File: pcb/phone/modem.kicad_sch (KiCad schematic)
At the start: 5 parts, among them U2 PCIE-52P40H_C444926, U8 TXB0108PWR

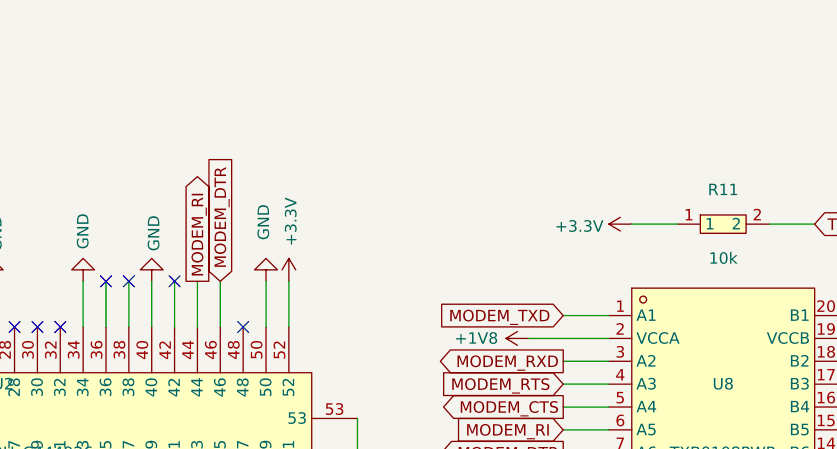
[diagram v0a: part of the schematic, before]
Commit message: Add deferred components: VBUS divider, MCU_MODEM_PWR_EN pull-down, SWD header, NET_STATUS LED
MCU sheet:
- R11 (10k): MCU_MODEM_PWR_EN pull-down to GND
- R12 (100k) + R13 (47k): VBUS_SENSE voltage divider from VBUS to GND
- J3 (Conn_01x04): SWD programming header (SWCLK, SWDIO, +3.3V, GND)
- Removed 4 no_connect markers (MCU_MODEM_PWR_EN, VBUS_SENSE, SWCLK, SWDIO)

Modem sheet:
- R12 (1k) + LED1 (LTST-C191TBKT): NET_STATUS indicator LED
- Removed 1 no_connect marker (NET_STATUS)

ERC: 0 errors, 4 warnings (all lib_symbol_mismatch — 3 pre-existing + 1 new for J3)

Generated with [Devin](https://devin.ai)

Co-Authored-By: Devin <158243242+devin-ai-integration[bot]@users.noreply.github.com>
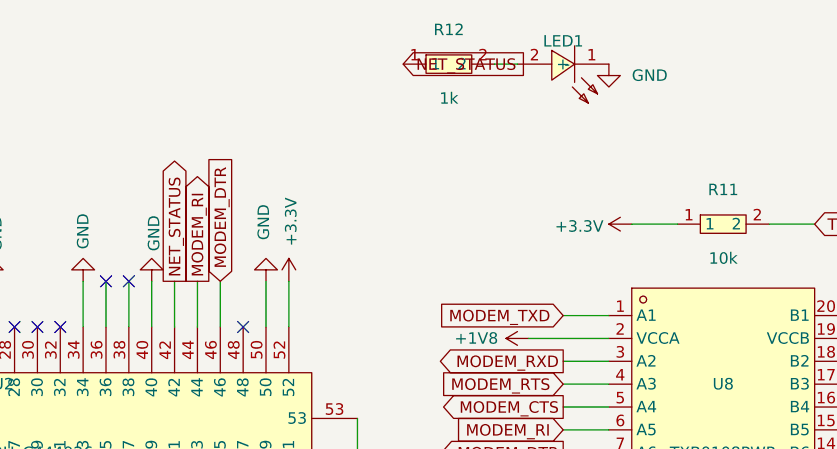
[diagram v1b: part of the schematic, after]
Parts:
- added LED1: LTST-C191TBKT, easyeda2kicad:LED0603-RD, symbol passives:LTST-C191TBKT
- added R12: 1k, symbol passives:RC0603JR-0710KL
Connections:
- net GND: now also LED1.1 (-)
- net NET_STATUS: now reaches U2.42
- net NET_STATUS: now also R12.1
- new net: LED1.2 (+), R12.2
- no-connect marks 17 -> 16

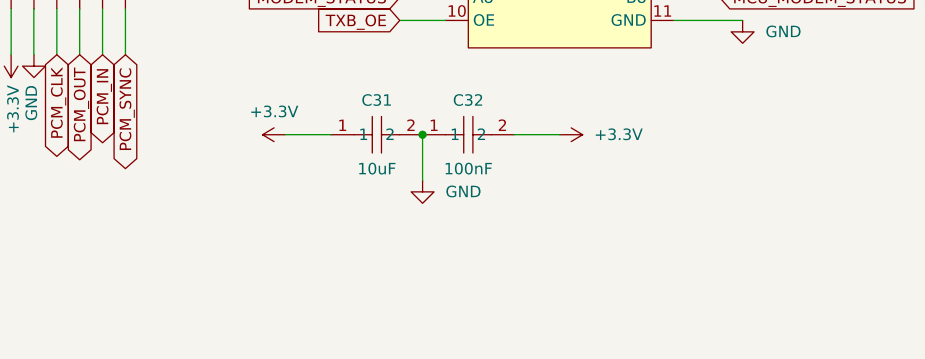
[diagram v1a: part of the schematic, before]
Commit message: Add power slide switch, modem bulk caps, reverse load switch decision
- SW1 (ALPS SSSS811101) added to power sheet: controls TPS63021 EN pin
  (ON: +BATT->R1->SW1->EN, OFF: EN->SW1->GND). Allows charging while off.
- C40 (470uF tantalum) + C41/C42 (10uF ceramic) added to modem sheet
  near MPCIe VCC pins for 2A+ LTE burst handling.
- Reversed load switch decision: SIM7600 sleep mode + PWRKEY make it
  redundant. Removed R11 (MCU_MODEM_PWR_EN pull-down), added no_connect
  on PE6.
- Registered temp_switch/temp_470uf/temp_10uf libraries in sym-lib-table
  and fp-lib-table (resolves 3 library-link ERC warnings).
- Final ERC: 0 errors, 6 warnings (all lib_symbol_mismatch, harmless).
- Updated docs: project-log, task-tracker, bom.

Generated with [Devin](https://devin.ai)

Co-Authored-By: Devin <158243242+devin-ai-integration[bot]@users.noreply.github.com>
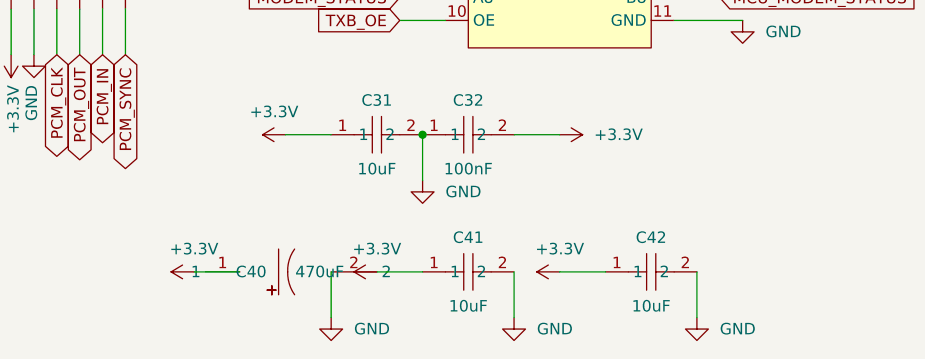
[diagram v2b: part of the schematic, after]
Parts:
- added C40: 470uF, symbol temp_470uf:6TPF470MAH
- added C41, C42: 10uF, symbol passives:GRM21BR61H106KE43L
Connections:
- net +3.3V: now also C40.1, C41.1, C42.1
- net GND: now also C40.2, C41.2, C42.2

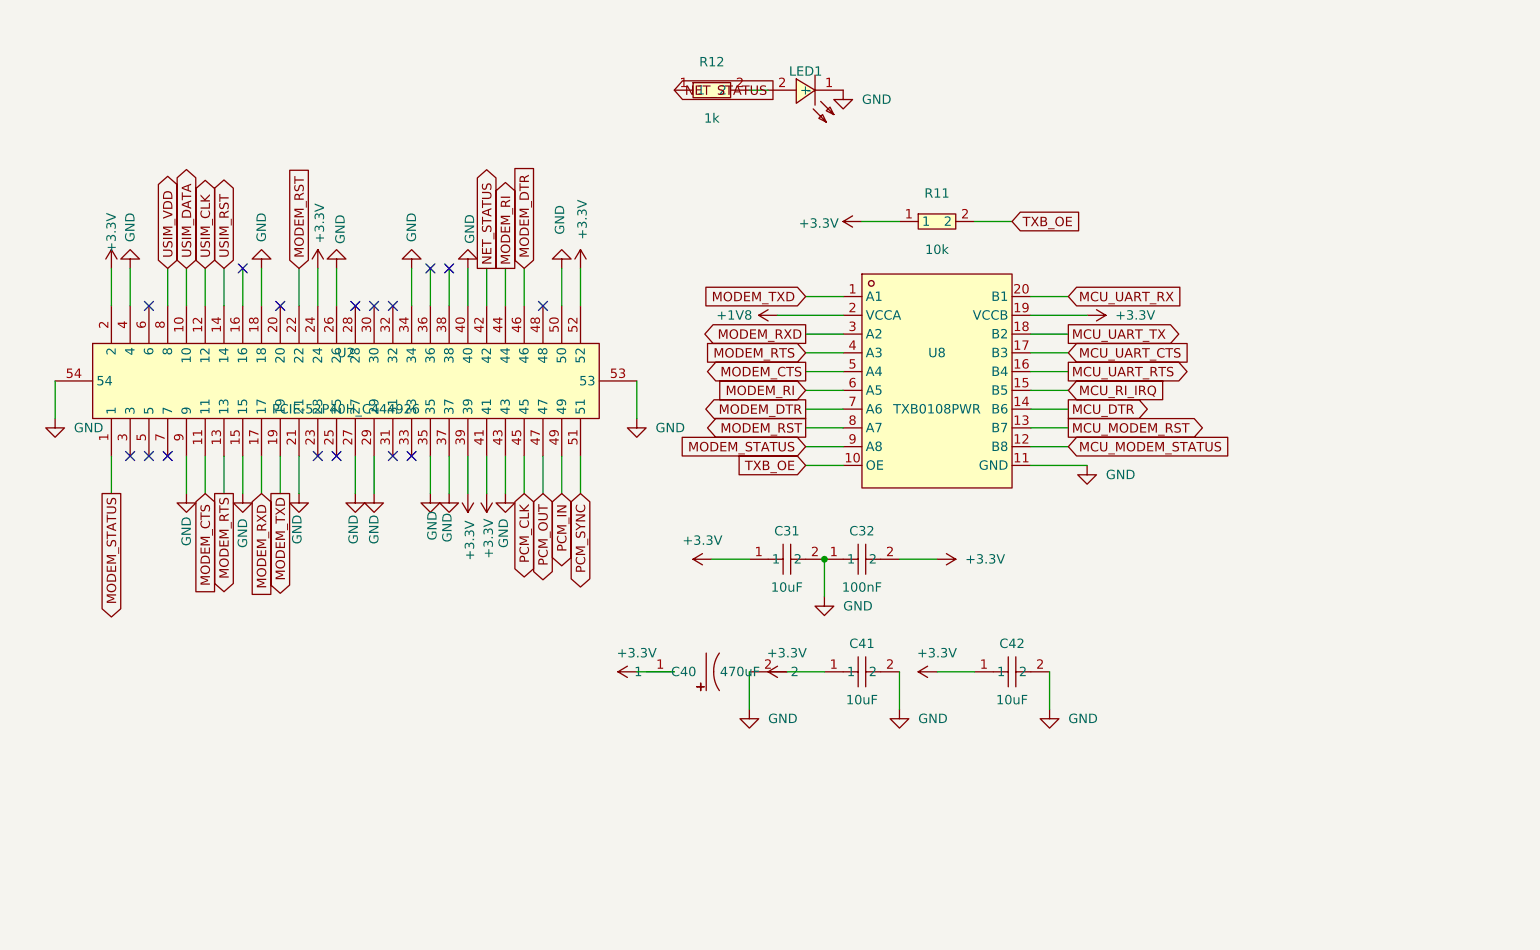
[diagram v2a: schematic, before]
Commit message: Cleanup: remove rejected part symbols, one-off scripts, stale datasheets
- Remove 7 rejected symbols from easyeda2kicad.kicad_sym (PJ-327C-4A,
  PJ-3250-5A, PJ-3240-5A, TYPE-C16PLC-H10.0, PJ-327A5JJ, PJ-327-P5,
  TYPEC-306DDW-ARP16) — replaced by Tensility 54-00298 and GCT USB4085-GF-A
- Delete 10 one-off inspection scripts (check_*.py, find_*.py, dump_*.py,
  extract_*.py) — keep only gen_*.py schematic generators
- Delete rejected datasheets (pj3126-5a, pj3240-5a, pj3250-5a, pj3f07-5p,
  N114 superseded display)
- Delete generated BOM/POS CSV files
- Add alps-ssss2.pdf and gct-usb4085.pdf to reference README index
- Include all schematic changes from previous sessions (SD pullups, VBUS
  divider fix, level shifter verification, codec caps, DCVDD fix)

Generated with [Devin](https://devin.ai)

Co-Authored-By: Devin <158243242+devin-ai-integration[bot]@users.noreply.github.com>
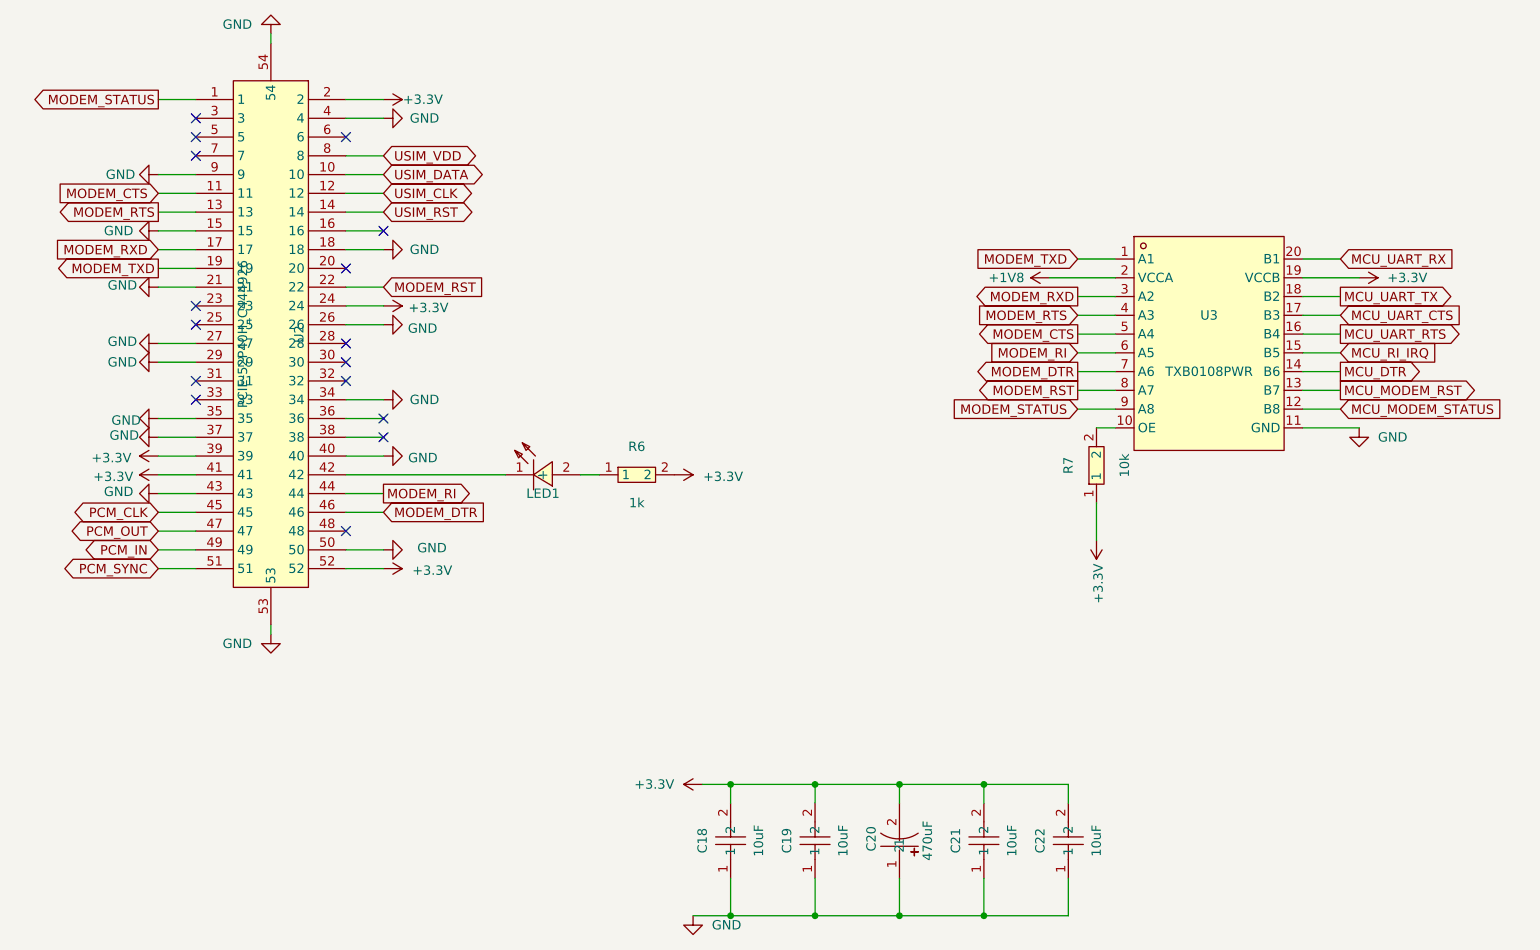
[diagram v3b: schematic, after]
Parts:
- removed C31, C41, C42: 10uF, symbol passives:GRM21BR61H106KE43L
- removed C32: 100nF, symbol passives:CC0603KRX7R9BB104
- removed C40: 470uF, symbol temp_470uf:6TPF470MAH
- added C18, C19, C21, C22: 10uF, symbol passives:GRM21BR61H106KE43L
- added C20: 470uF, symbol temp_470uf:6TPF470MAH
- renumbered R12 to R6, R11 to R7, U8 to U3
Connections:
- net +3.3V: now also R6.2, C18.2, C19.2, C20.2, C21.2, C22.2
- net GND: now also C18.1, C19.1, C20.1, C21.1, C22.1; no longer LED1.1 (-)
- net at LED1.2 (+): now also R6.1; no longer R6.2
- net NET_STATUS: no longer names the net of U2.42
- net NET_STATUS: now also LED1.1 (-); no longer R6.1
- net TXB_OE: no longer names the net of R7.2, U3.10 (OE)
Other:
- moved on the sheet: LED1, R6, R7, U2, U3

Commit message: Sync docs to schematic refdes + add VDDA ferrite, C20 footprint, completion plan
- Sync 11 doc files to schematic-canonical reference designators (U3->U5 codec,
  U4->U8 buck-boost, U5->U9 LDO, U6->U11 charger, U7->U10 fuel gauge, U8->U3
  TXB0108, U9->U12 SN74AXC4T774, U10->D1 USBLC6-2, U11->U6/U7 ESDA6V1,
  J1->USBC1, J_BATT->CN1, SW1->SW21). Schematic refdes are canonical.
- MCU sheet: add VDDA ferrite bead (L1 BLM18KG601SN1D) + 1uF (C18) + 10nF (C19)
  decoupling per datasheet. Add PWR_FLAG on VDDA for ERC.
- Modem sheet: assign C20 (470uF tantalum) footprint temp_470uf:CAP-SMD_L7.3-W4.3
- Libraries: add new symbols to easyeda2kicad.kicad_sym + passives.kicad_sym
- Add .devin/rules/kicad-mcp-first.md (MCP-first inspection rule)
- Add docs/schematic-completion-plan.md (per-sheet review tracker, 2026-07-28)
- Add pcb/phone/scripts/add_headphone_jack.py (flagged for cleanup in plan §D)

Generated with [Devin](https://devin.ai)

Co-Authored-By: Devin <158243242+devin-ai-integration[bot]@users.noreply.github.com>
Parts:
- C20: footprint (none) -> temp_470uf:CAP-SMD_L7.3-W4.3
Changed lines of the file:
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@@
 			)
 		)
-		(property "Footprint" ""
+		(property "Footprint" "temp_470uf:CAP-SMD_L7.3-W4.3"
 			(at 175.26 162.56 0)
 			(hide yes)

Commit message: Project file audit cleanup: delete stale files, merge temp libs, fix docs
Delete stale/duplicate/garbage files identified by full project audit:
- easyeda2kicad.kicad_sym + missing_parts.kicad_sym (stale 1-symbol
  duplicates of symbols already in main libs; rebuild workflow broken)
- rebuild_lib.py + update_sch_refs.py + extract_pins.py (one-time
  migration scripts that no longer work — source files deleted)
- add_headphone_jack.py (dangerous — wiped codec sheet 2026-07-28)
- check_desc.py (one-off utility referencing stale file)
- main.kicad_sch (empty orphan, not referenced by project)
- bom_run.csv + 12 erc_*.txt + 2 ~*.lck (regenerable KiCad output)

Merge temp libraries into main libs (temp_switch/temp_470uf/temp_10uf):
- SSSS811101 slide switch -> electromech.kicad_sym
- 6TPF470MAH tantalum polymer -> passives.kicad_sym
- Footprints + 3D models moved to easyeda2kicad.pretty/3dshapes
- temp_10uf (CL10A106KP8NNNC) deleted — part was never placed
- Updated sym-lib-table, fp-lib-table, schematic lib_id/Footprint refs
- ERC validated: 0 errors, 15 warnings (all pre-existing types)

Fix documentation:
- lib/AGENTS.md: rewrote to reflect current state (4 libs are source
  of truth, no rebuild workflow, temp libs merged)
- .gitignore: removed 4 stale entries for gen_*.py at wrong paths
- research-notes.md: 3 [ ] -> [x] on RESOLVED items
- project-log.md: supersede note on 2026-07-22 entry + new audit entry
- datasheets/README.md: alps-ssss2.pdf -> alps-ssss8.pdf (wrong series
  datasheet — SSSS811101 is SSSS8 Series, not SSSS2; wrong LCSC # too)
- Downloaded correct alps-ssss8.pdf, deleted wrong alps-ssss2.pdf

Generated with [Devin](https://devin.ai)

Co-Authored-By: Devin <158243242+devin-ai-integration[bot]@users.noreply.github.com>
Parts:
- C20: footprint temp_470uf:CAP-SMD_L7.3-W4.3 -> easyeda2kicad:CAP-SMD_L7.3-W4.3; symbol temp_470uf:6TPF470MAH -> passives:6TPF470MAH
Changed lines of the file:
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@@
 	(symbol
 		(lib_name "6TPF470MAH_1")
-		(lib_id "temp_470uf:6TPF470MAH")
+		(lib_id "passives:6TPF470MAH")
 		(at 175.26 162.56 180)
 		(unit 1)
@@
 			)
 		)
-		(property "Footprint" "temp_470uf:CAP-SMD_L7.3-W4.3"
+		(property "Footprint" "easyeda2kicad:CAP-SMD_L7.3-W4.3"
 			(at 175.26 162.56 0)
 			(hide yes)

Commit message: Assign footprints to 29 components missing footprint properties
All 28 custom-library components (passives, connectors, ICs) get footprints
from their symbol library defaults. J1 (SWD debug header) gets a standard
KiCad 2.54mm through-hole pin header footprint per user selection.

Footprints assigned:
- C18-C23: easyeda2kicad:C0805 (10uF 0805 caps)
- C24-C26: easyeda2kicad:C0603 (100nF 0603 caps)
- R6-R18: easyeda2kicad:R0603 (0603 resistors)
- J_HINGE2: easyeda2kicad:FPC-SMD_14P-P0.50_HDGC_0.5K-HX-14PWB
- J_MIC1, J_SPK1: easyeda2kicad:CONN-SMD_P2.00_S2B-PH-SM4-TB-LF-SN
- U2: easyeda2kicad:PCIE-SMD_PCIE-52P40H-1 (mini-PCIe)
- U3: easyeda2kicad:TSSOP-20_L6.5-W4.4-P0.65-LS6.4-BL (TXB0108)
- U5: easyeda2kicad:QFN-40_L5.0-W5.0-P0.40-BL-EP3.7 (ALC5651)
- J1: Connector_PinHeader_2.54mm:PinHeader_1x04_P2.54mm_Vertical (SWD)

Also includes KiCad's own metadata updates (title block, sheet ordering,
designator list normalization).

Generated with [Devin](https://devin.ai)

Co-Authored-By: Devin <158243242+devin-ai-integration[bot]@users.noreply.github.com>
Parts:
- C18, C19, C21, C22: footprint (none) -> easyeda2kicad:C0805
- R6, R7: footprint (none) -> easyeda2kicad:R0603
- U2: footprint (none) -> easyeda2kicad:PCIE-SMD_PCIE-52P40H-1
- U3: footprint (none) -> easyeda2kicad:TSSOP-20_L6.5-W4.4-P0.65-LS6.4-BL
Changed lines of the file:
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@@
 			)
 		)
-		(property "Footprint" ""
+		(property "Footprint" "easyeda2kicad:R0603"
 			(at 201.93 111.76 0)
 			(hide yes)
@@
 			)
 		)
-		(property "Footprint" ""
+		(property "Footprint" "easyeda2kicad:R0603"
 			(at 139.7 113.03 0)
 			(hide yes)
@@
 			)
 		)
-		(property "Footprint" ""
+		(property "Footprint" "easyeda2kicad:C0805"
 			(at 163.83 162.56 0)
 			(hide yes)
@@
 			)
 		)
-		(property "Footprint" ""
+		(property "Footprint" "easyeda2kicad:TSSOP-20_L6.5-W4.4-P0.65-LS6.4-BL"
 			(at 217.17 95.25 0)
 			(hide yes)
@@
 			)
 		)
-		(property "Footprint" ""
+		(property "Footprint" "easyeda2kicad:PCIE-SMD_PCIE-52P40H-1"
 			(at 90.17 93.98 0)
 			(hide yes)
@@
 			)
 		)
-		(property "Footprint" ""
+		(property "Footprint" "easyeda2kicad:C0805"
 			(at 152.4 162.56 0)
 			(hide yes)
@@
 			)
 		)
-		(property "Footprint" ""
+		(property "Footprint" "easyeda2kicad:C0805"
 			(at 198.12 162.56 0)
 			(hide yes)
@@
 			)
 		)
-		(property "Footprint" ""
+		(property "Footprint" "easyeda2kicad:C0805"
 			(at 186.69 162.56 0)
 			(hide yes)
